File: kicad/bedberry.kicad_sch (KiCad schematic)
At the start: 44 parts, among them J1 629105150521, J2 SJ1-3533NG, P1 RPi Zero 2 W, Q1 BC817, Q2 IRLML2246TRPBF, Q3 BC817, U1 TSOP382xx, U11 CAT24C128

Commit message: Small updates/descriptions
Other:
- note added: "BEDBERRY v1.0"
- note added: "Raspberry PI Zero 2W This will be mounted inverted on the PCB to reduce height and allow for thermal linking between CPU and base board."
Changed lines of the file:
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@@
+    (effects (font (size 1.27 1.27)) (justify left bottom))
+  )
+  (text "Raspberry PI Zero 2W\n\nThis will be mounted inverted\non the PCB to reduce height and\nallow for thermal linking between \nCPU and base board."
+    (at 130.81 74.93 0)
     (effects (font (size 1.27 1.27)) (justify left bottom))
   )
@@
     (effects (font (size 1.27 1.27)) (justify left bottom))
   )
+  (text "BEDBERRY v1.0" (at 181.61 177.8 0)
+    (effects (font (size 4 4)) (justify left bottom))
+  )
   (label "GPIO5_AUX_OUT" (at 95.25 124.46 0)

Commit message: updated design
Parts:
- removed D1: MP001251, LED_SMD:LED_Avago_PLCC4_3.2x2.8mm_CW, symbol LED:ASMB-MTB0-0A3A2
- added D1: KPFA-3010RGBC-11, LED_SMD:LED_Kingbright_APFA3010_3x1.5mm_Horizontal, symbol LED:APFA3010
- C1: EuroCircuits (none) -> GPC0805102; JLCPCB (none) -> CL21B102KBCNNNC; LCSC (none) -> C46653
- C19: value 100uF 8mm TH -> 100uF 10mm TH; footprint Capacitor_THT:CP_Radial_D8.0mm_P3.50mm -> Capacitor_THT:CP_Radial_D10.0mm_P5.00mm
- C2, C20, C4: value 100nF 0805 -> 100nF 0603; footprint Capacitor_SMD:C_0805_2012Metric -> Capacitor_SMD:C_0603_1608Metric; EuroCircuits (none) -> GPC0603104; JLCPCB (none) -> CC0603KRX7R9BB104; LCSC (none) -> C14663
- C5, C6, C7: EuroCircuits (none) -> GPC0805105; JLCPCB (none) -> CL21B105KBFNNNE; LCSC (none) -> C28323
- D2, D3: EuroCircuits (none) -> LTE-4206
- F1: EuroCircuits (none) -> MP005240; JLCPCB (none) -> SMD1812P300TF/16V; LCSC (none) -> C55996
- F2: EuroCircuits (none) -> 1206L150THWR; JLCPCB (none) -> SMD1206P050TF/24; LCSC (none) -> C209741
- J1: value 629105150521 -> USB Micro-B; footprint Connector_USB:USB_Micro-B_Molex_47346-0001 -> Connector_USB:USB_Micro-B_Amphenol_10118194_Horizontal; EuroCircuits (none) -> 10118194-0001LF; JLCPCB (none) -> 10118194-0001LF; LCSC (none) -> C132563
- J2: EuroCircuits (none) -> SJ1-3533NG
- P1: EuroCircuits (none) -> A-BL254-DG-G40D
- Q1, Q3: EuroCircuits (none) -> BC817-25LT1G; JLCPCB (none) -> BC817-25,215; LCSC (none) -> C39828
- Q2: value IRLML2246TRPBF -> MOSFET P-Ch; EuroCircuits (none) -> DMG2307L; JLCPCB (none) -> DMG2307L-7; LCSC (none) -> C102620
- R1: EuroCircuits (none) -> GPR08051M; JLCPCB (none) -> 0805W8F1004T5E; LCSC (none) -> C17514
- R16, R17, R18, R5, R8: EuroCircuits (none) -> GPR08051K; JLCPCB (none) -> 0805W8F1001T5E; LCSC (none) -> C17513
- R2: EuroCircuits (none) -> GPR0805120R; JLCPCB (none) -> 0805W8F1200T5E; LCSC (none) -> C17437
- R3, R4: EuroCircuits (none) -> GPR08055R6; JLCPCB (none) -> 0805W8J056JT5E; LCSC (none) -> C25321
- R6, R9: value 12 -> 5.6; EuroCircuits (none) -> GPR08055R6; JLCPCB (none) -> 0805W8J056JT5E; LCSC (none) -> C25321
- R7: value 22k -> 10k; EuroCircuits (none) -> GPR080510K; JLCPCB (none) -> 0805W8F1002T5E; LCSC (none) -> C17414
- TP1, TP2, TP3, TP4, TP5: EuroCircuits (none) -> 5006
- U1: EuroCircuits (none) -> TSOP38238
- U11: EuroCircuits (none) -> CAT24C128WI-GT3; JLCPCB (none) -> CAT24C128WI-GT3; LCSC (none) -> C81195
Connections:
- net +3V3: now also D1.2 (A)
- net at R3.1: now also D1.3 (G)
- net at R4.1: now also D1.4 (B)
- net at R2.1: now also D1.1 (R)
- net GPIO23(GEN4) renamed GPIO23_RESET
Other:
- sheet IO_Bed ports: added ~{RESET}; removed none
- moved on the sheet: TP5

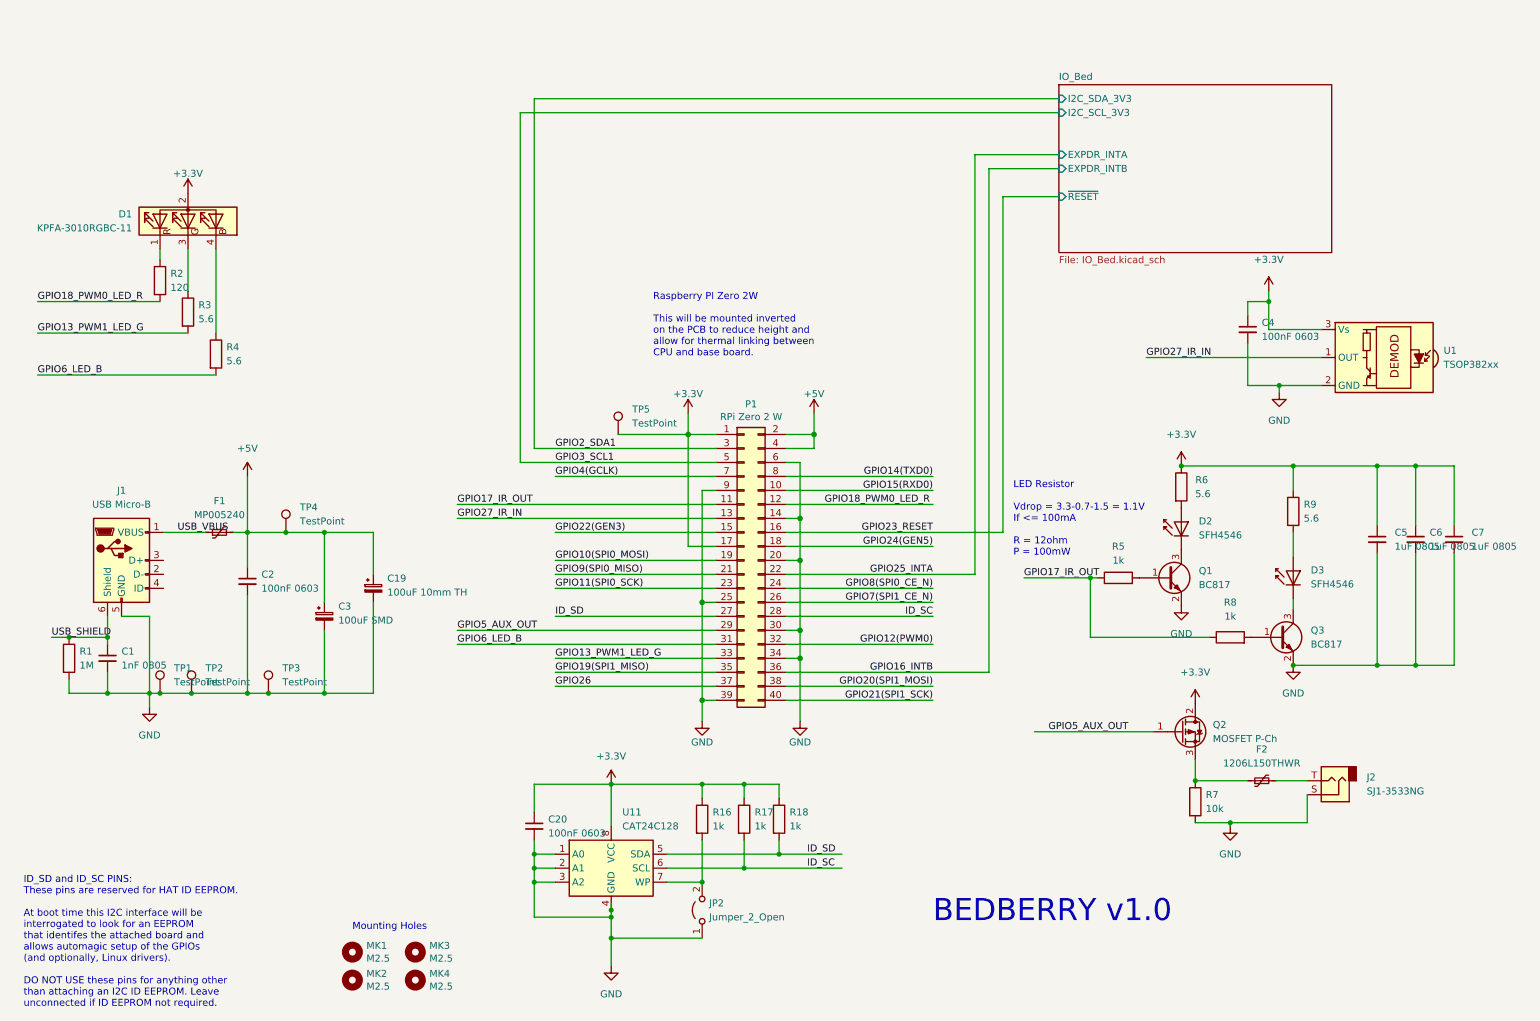
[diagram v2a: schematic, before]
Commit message: BOM changes; RPi thermal gap
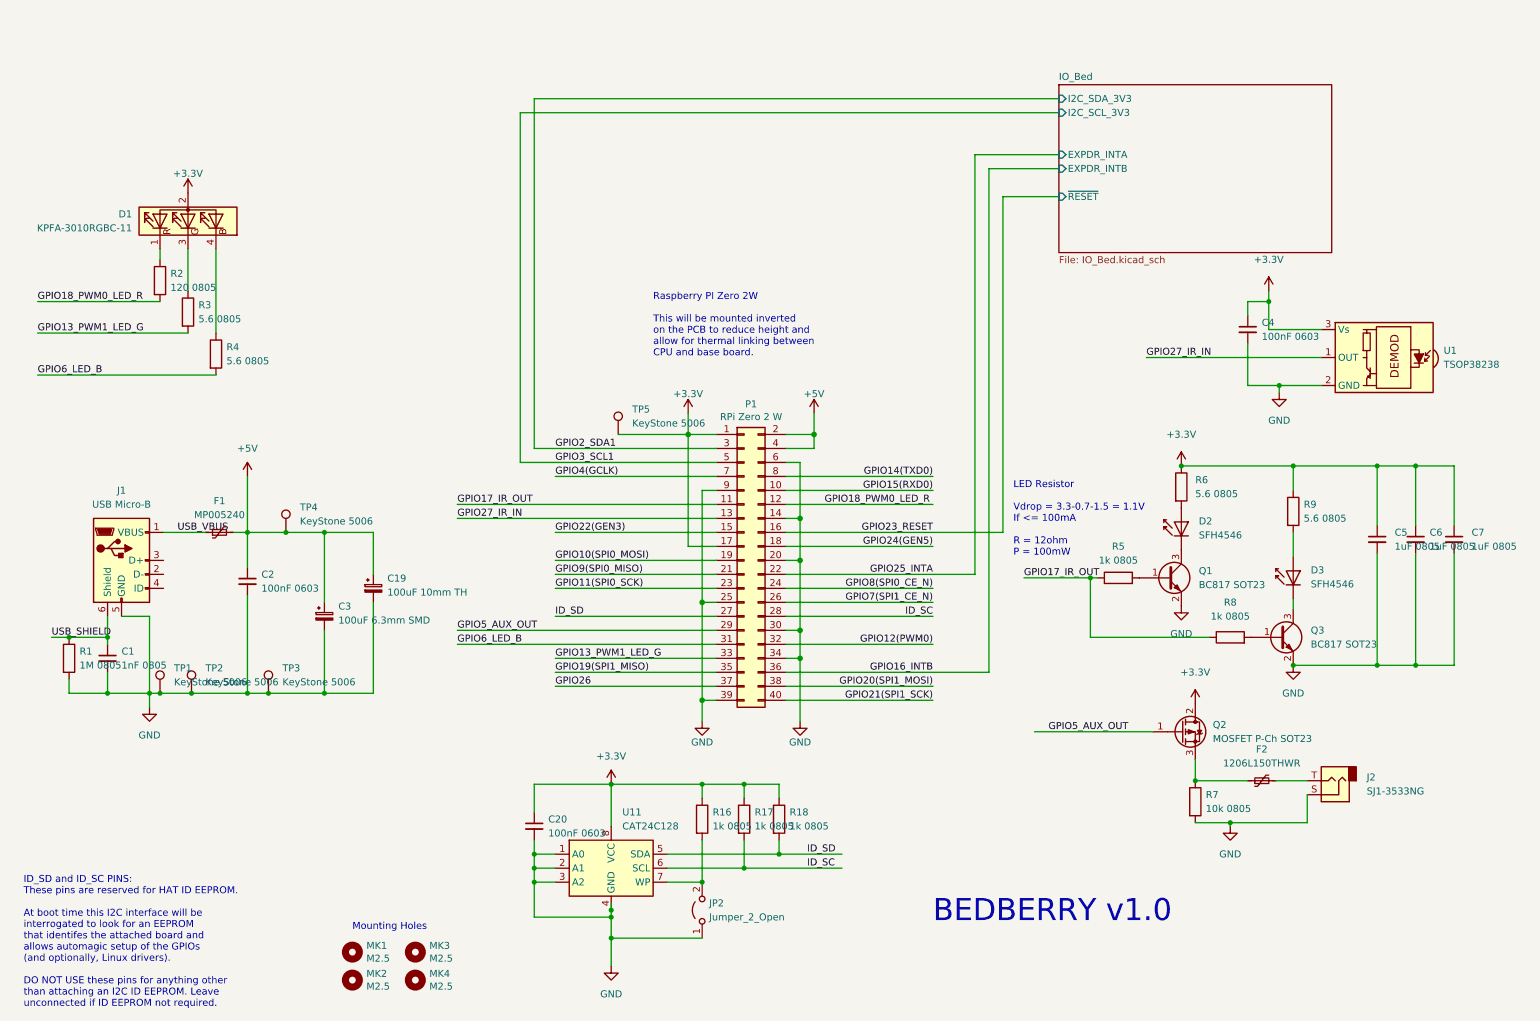
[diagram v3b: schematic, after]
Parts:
- C19, C5, C6, C7, MK1, MK2, MK3, MK4: DNS (none) -> X
- C3: value 100uF SMD -> 100uF 6.3mm SMD; DNS (none) -> X
- D1: MPN (none) -> KPFA-3010RGBC-11
- D2, D3: DNS (none) -> X; MPN (none) -> LTE-4206
- F1: MPN (none) -> MP005240
- F2: MPN (none) -> 1206L150THWR
- J1: MPN (none) -> 10118194-0001LF
- J2: DNS (none) -> X; MPN (none) -> SJ1-3533NG
- P1: DNS (none) -> X; MPN (none) -> A-BL254-DG-G40D
- Q1, Q3: value BC817 -> BC817 SOT23; MPN (none) -> BC817-25LT1G
- Q2: value MOSFET P-Ch -> MOSFET P-Ch SOT23; MPN (none) -> DMG2307L-7
- R1: value 1M -> 1M 0805
- R16, R17, R18, R5, R8: value 1k -> 1k 0805
- R2: value 120 -> 120 0805
- R3, R4, R6, R9: value 5.6 -> 5.6 0805
- R7: value 10k -> 10k 0805
- TP1, TP2, TP3, TP4, TP5: value TestPoint -> KeyStone 5006; DNS (none) -> X; MPN (none) -> 5006
- U1: value TSOP382xx -> TSOP38238; DNS (none) -> X; MPN (none) -> TSOP38238
- U11: MPN (none) -> CAT24C128WI-GT3

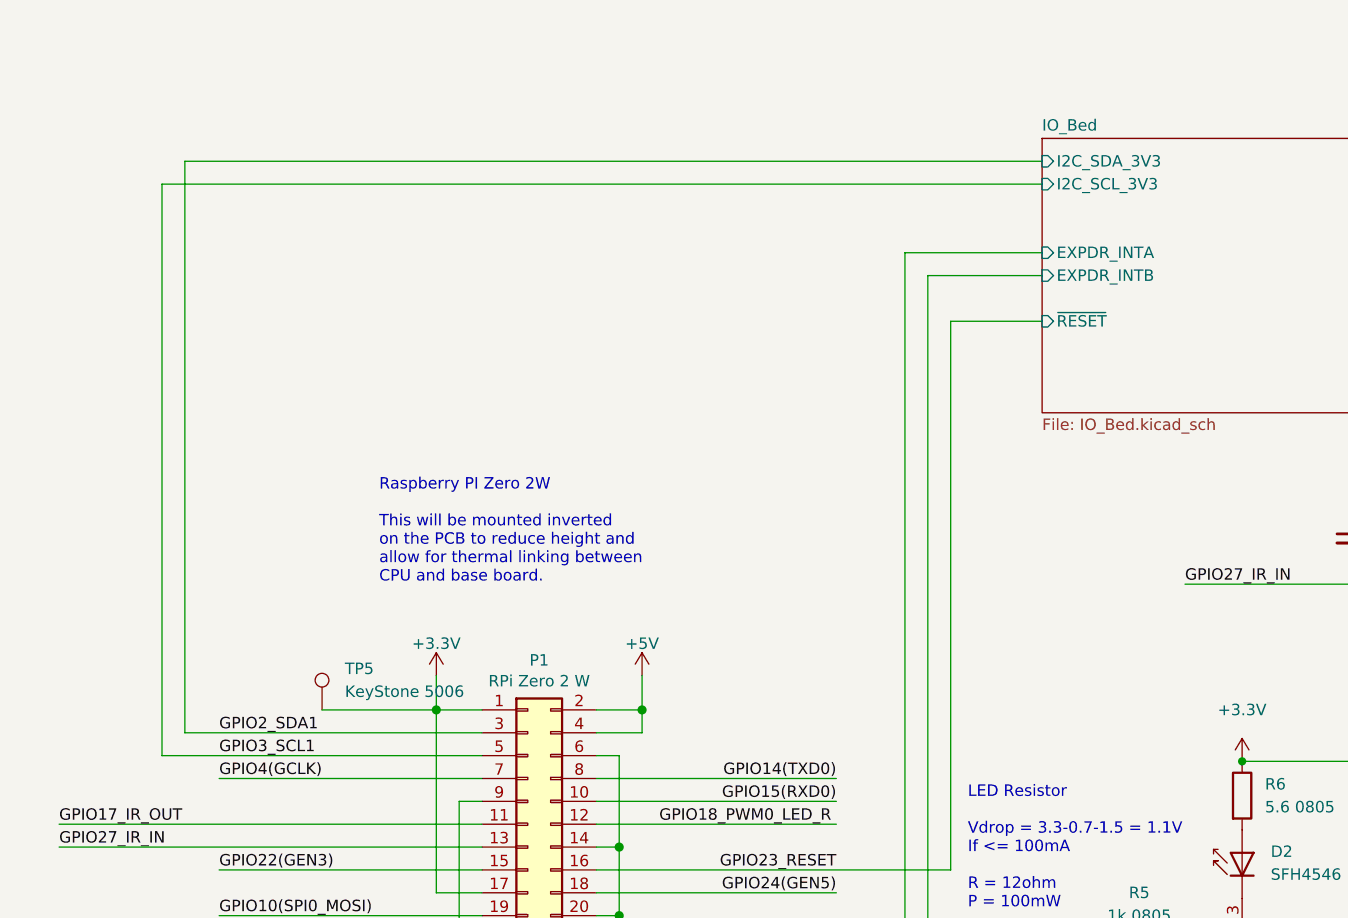
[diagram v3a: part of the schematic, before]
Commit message: start changing relays
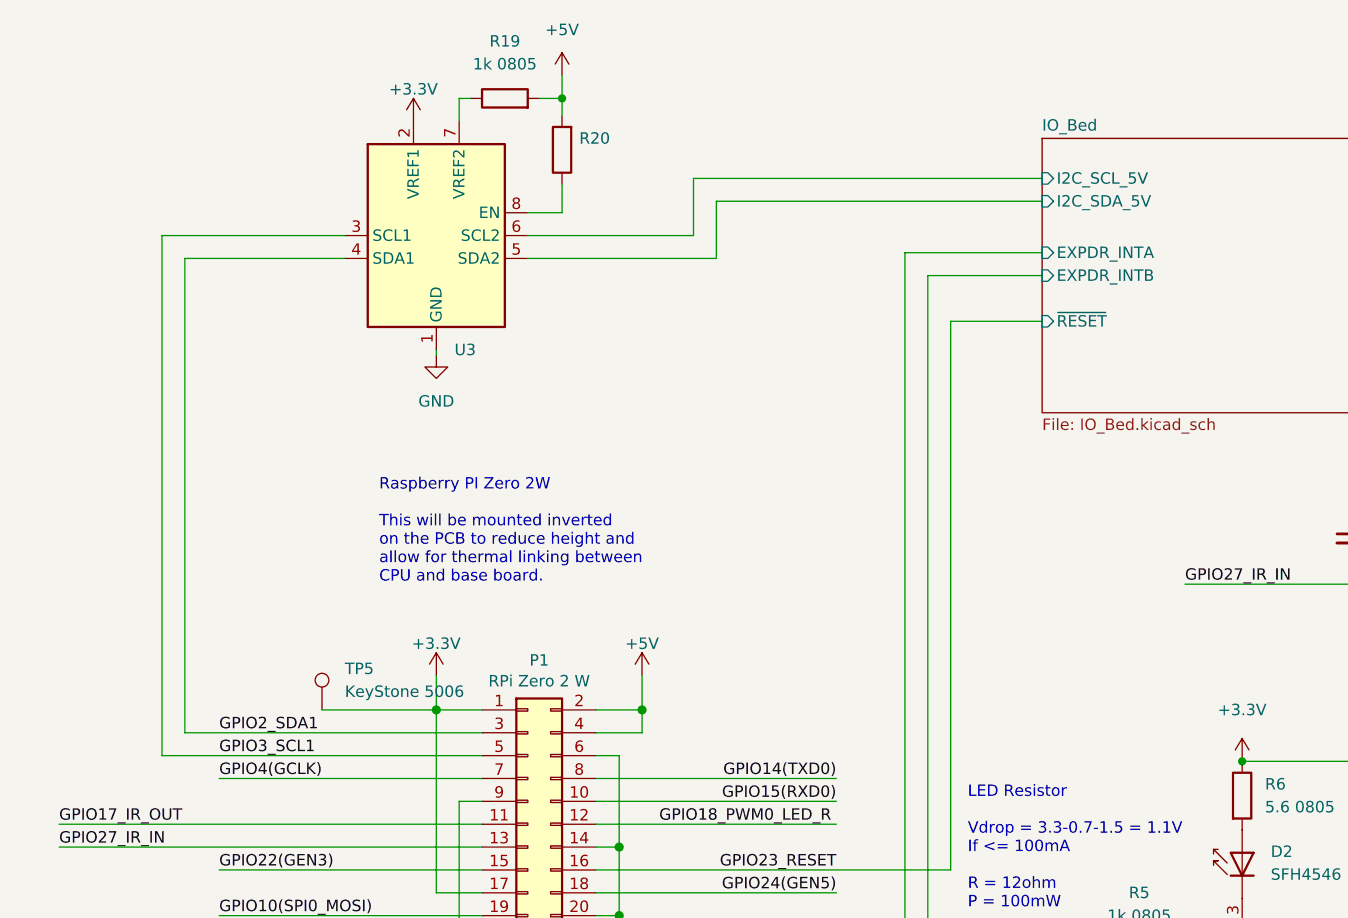
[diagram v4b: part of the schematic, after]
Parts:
- added R19: 1k 0805, Resistor_SMD:R_0805_2012Metric, symbol Device:R
- added R20: (no value), symbol Device:R
- added U3: (no value), symbol Interface:PCA9306D
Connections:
- net +3V3: now also U3.2 (VREF1)
- net +5V: now also R19.2, R20.2
- net GND: now also U3.1 (GND)
- net GPIO2_SDA1: now also U3.4 (SDA1)
- net GPIO3_SCL1: now also U3.3 (SCL1)
- new net: R20.1, U3.8 (EN)
- new net: R19.1, U3.7 (VREF2)
- new net IO_Bed/I2C_SCL_5V: U3.6 (SCL2)
- new net IO_Bed/I2C_SDA_5V: U3.5 (SDA2)
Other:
- sheet IO_Bed ports: added I2C_SCL_5V, I2C_SDA_5V; removed I2C_SCL_3V3, I2C_SDA_3V3
